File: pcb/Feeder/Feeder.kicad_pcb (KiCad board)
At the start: 2 copper layers, 19.8 x 10.8 mm, 5 parts, among them J1 Controller, J2 Servo, J3 Feedback, J4 N20

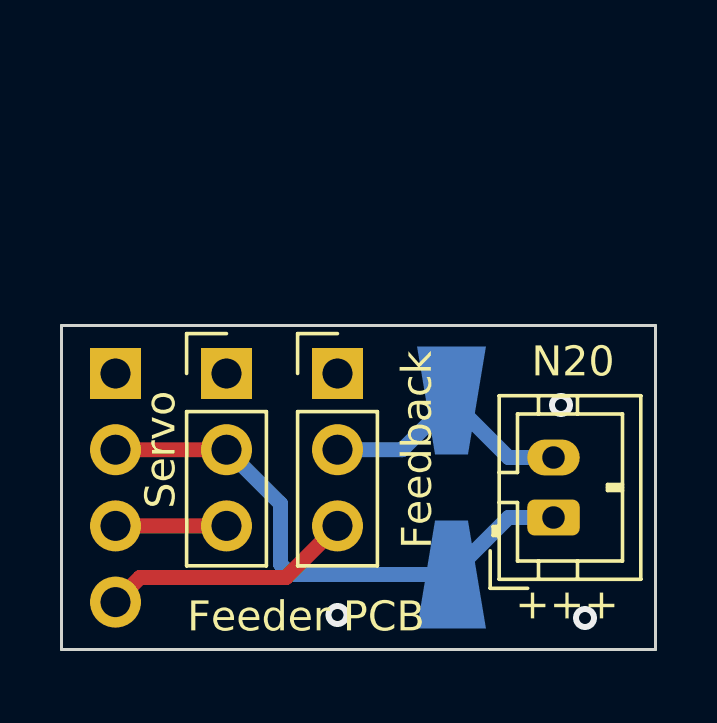
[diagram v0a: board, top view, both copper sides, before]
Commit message: Update Feeder PCB to adjust footprints for clearances.
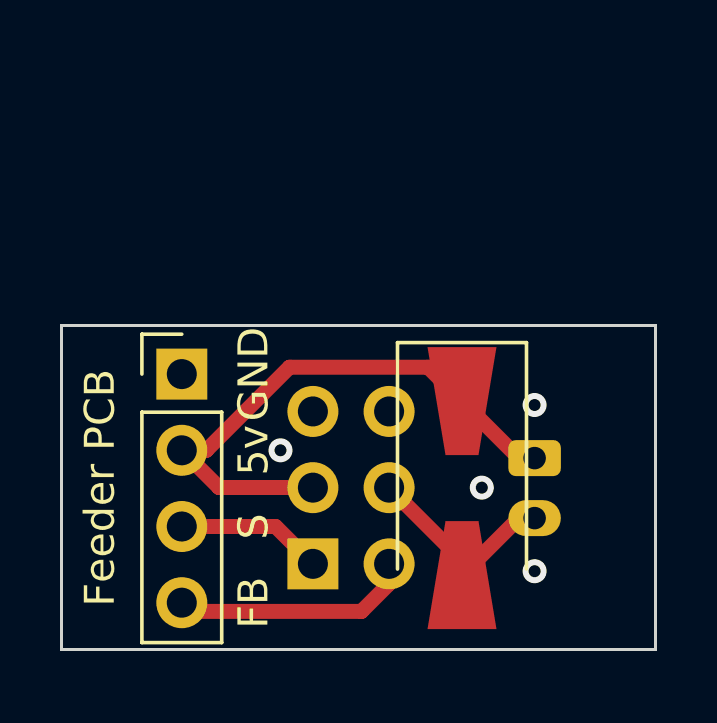
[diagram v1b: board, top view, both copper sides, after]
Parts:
- removed J4: N20, Connector_JST:JST_PH_B2B-PH-K_1x02_P2.00mm_Vertical
- D1, J1: moved to F.Cu
- J2: value Servo -> N20; footprint Connector_PinHeader_2.54mm:PinHeader_1x03_P2.54mm_Vertical -> Connector_JST:JST_PH_B2B-PH-K_1x02_P2.00mm_Vertical; moved to B.Cu
- J3: value Feedback -> Servo/Feedback; footprint Connector_PinHeader_2.54mm:PinHeader_1x03_P2.54mm_Vertical -> Connector_PinHeader_2.54mm:PinHeader_2x03_P2.54mm_Vertical; moved to B.Cu
- moved J2 10.7 mm to (153.9, 93.2), turned to -90 degrees
- moved J3 6.40 mm to (146.5, 96.7)
- moved J1 2.21 mm to (142.1, 90.4), turned to 0 degrees
- moved D1 0.35 mm to (151.4, 94.2), turned to -90 degrees
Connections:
- J2 pad 1: GND -> +5V
- J2 pad 2: +5V -> /N20-GND
- J3 pad 1: GND -> /SERVO
- J3 pad 2: /N20-GND -> /FEEDBACK
- J3 pad 3: /FEEDBACK -> +5V
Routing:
- net /N20-GND: track 8.67 -> 7.13 mm
- net /SERVO: track 3.70 -> 4.89 mm
- net +5V: track 18.3 -> 19.0 mm
- net GND: vias 3 -> 4

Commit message: Feeder - added optional THT diode footprint, repanelized
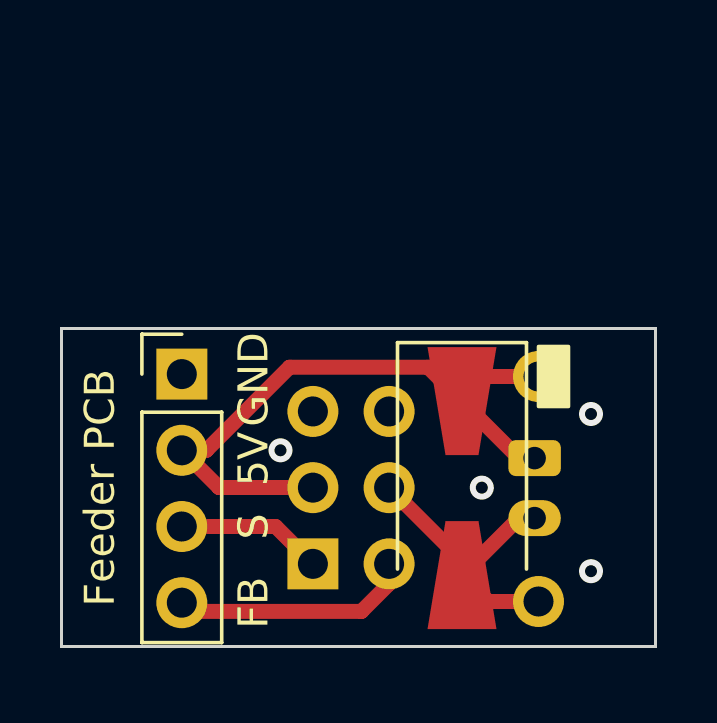
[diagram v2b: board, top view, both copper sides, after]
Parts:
- added D2: 1N4001, CustomDiode:D_SMA-SMB_Universal_Handsoldering_Holes, F.Cu at (154.0, 94.2)
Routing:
- net /N20-GND: track 7.13 -> 10.0 mm
- net +5V: track 19.0 -> 21.9 mm
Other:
- board size 19.8 x 10.8 mm -> 19.8 x 10.6 mm
- board text added: "+"
- board text added: "5V"
- board text removed: "+++"
- board text removed: "5v"
- board text removed: "JLCJLCJLCJLC"

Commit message: recreated feeder PCB for new 0816 CAD design (#5)
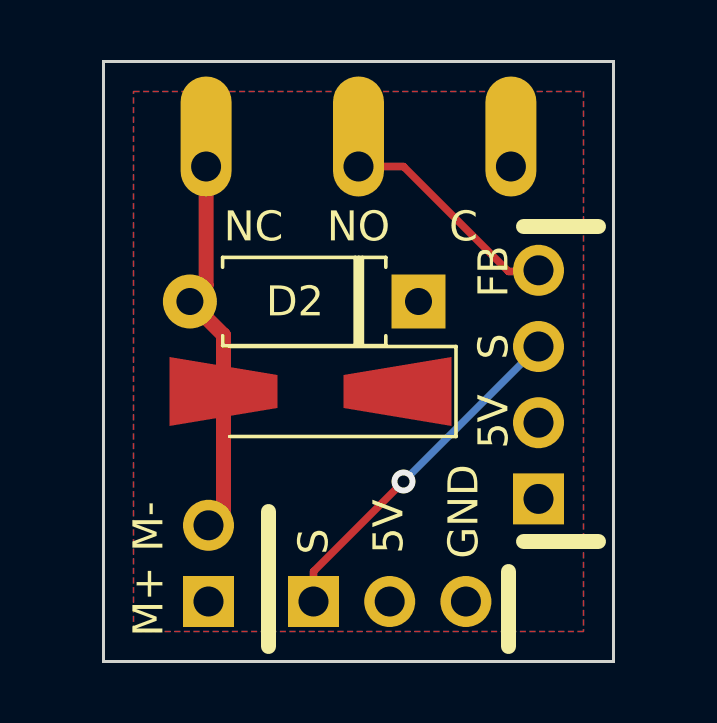
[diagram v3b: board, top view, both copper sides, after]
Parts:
- removed J3: Servo/Feedback, Connector_PinHeader_2.54mm:PinHeader_2x03_P2.54mm_Vertical
- added J4: Conn_01x04, PinsClean:PinSocket_1x04_P2.54mm_Vertical_Clean, F.Cu at (154.0, 94.6)
- added SW1: SW_SPDT, Microswitch:Microswitch, F.Cu at (153.1, 83.5)
- D2: footprint CustomDiode:D_SMA-SMB_Universal_Handsoldering_Holes -> Diode_THT:D_A-405_P7.62mm_Horizontal
- J1: value Controller -> Conn_01x03_Male; footprint Connector_PinHeader_2.54mm:PinHeader_1x04_P2.54mm_Vertical -> PinsClean:PinSocket_1x03_P2.54mm_Vertical_Clean
- J2: footprint Connector_JST:JST_PH_B2B-PH-K_1x02_P2.00mm_Vertical -> PinsClean:PinSocket_1x02_P2.54mm_Vertical_Clean; moved to F.Cu
- moved J2 11.9 mm to (143.0, 98.0), turned to 180 degrees
- moved J1 8.76 mm to (146.5, 98.0), turned to 90 degrees
- moved D2 7.42 mm to (150.0, 88.0), turned to 180 degrees
- moved D1 5.99 mm to (146.4, 91.0), turned to 180 degrees
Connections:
- J1 pad 1: GND -> /SERVO
- J1 pad 3: /SERVO -> GND
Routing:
- net +5V: track 21.9 -> 0.00 mm
- net /SERVO: track 4.89 -> 11.6 mm, vias 0 -> 1
- net /N20-GND: track 10.0 -> 12.9 mm
- net /FEEDBACK: track 8.08 -> 7.47 mm
- net GND: vias 4 -> 0
- added copper zone on F.Cu, net +5V
- removed copper zone on F.Cu, net GND
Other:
- board size 19.8 x 10.6 mm -> 17 x 20 mm
- board text added: "Feeder"
- board text added: "M+"
- board text added: "M-"
- board text added: "PCB"
- board text removed: "+"
- board text removed: "COM"
- board text removed: "Feeder PCB"
- board text removed: "NC"
- board text removed: "NO"
